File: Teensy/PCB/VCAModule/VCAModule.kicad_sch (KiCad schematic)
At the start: 11 parts, among them J1 Power_Connector_2x3, U1 Teensy4.0

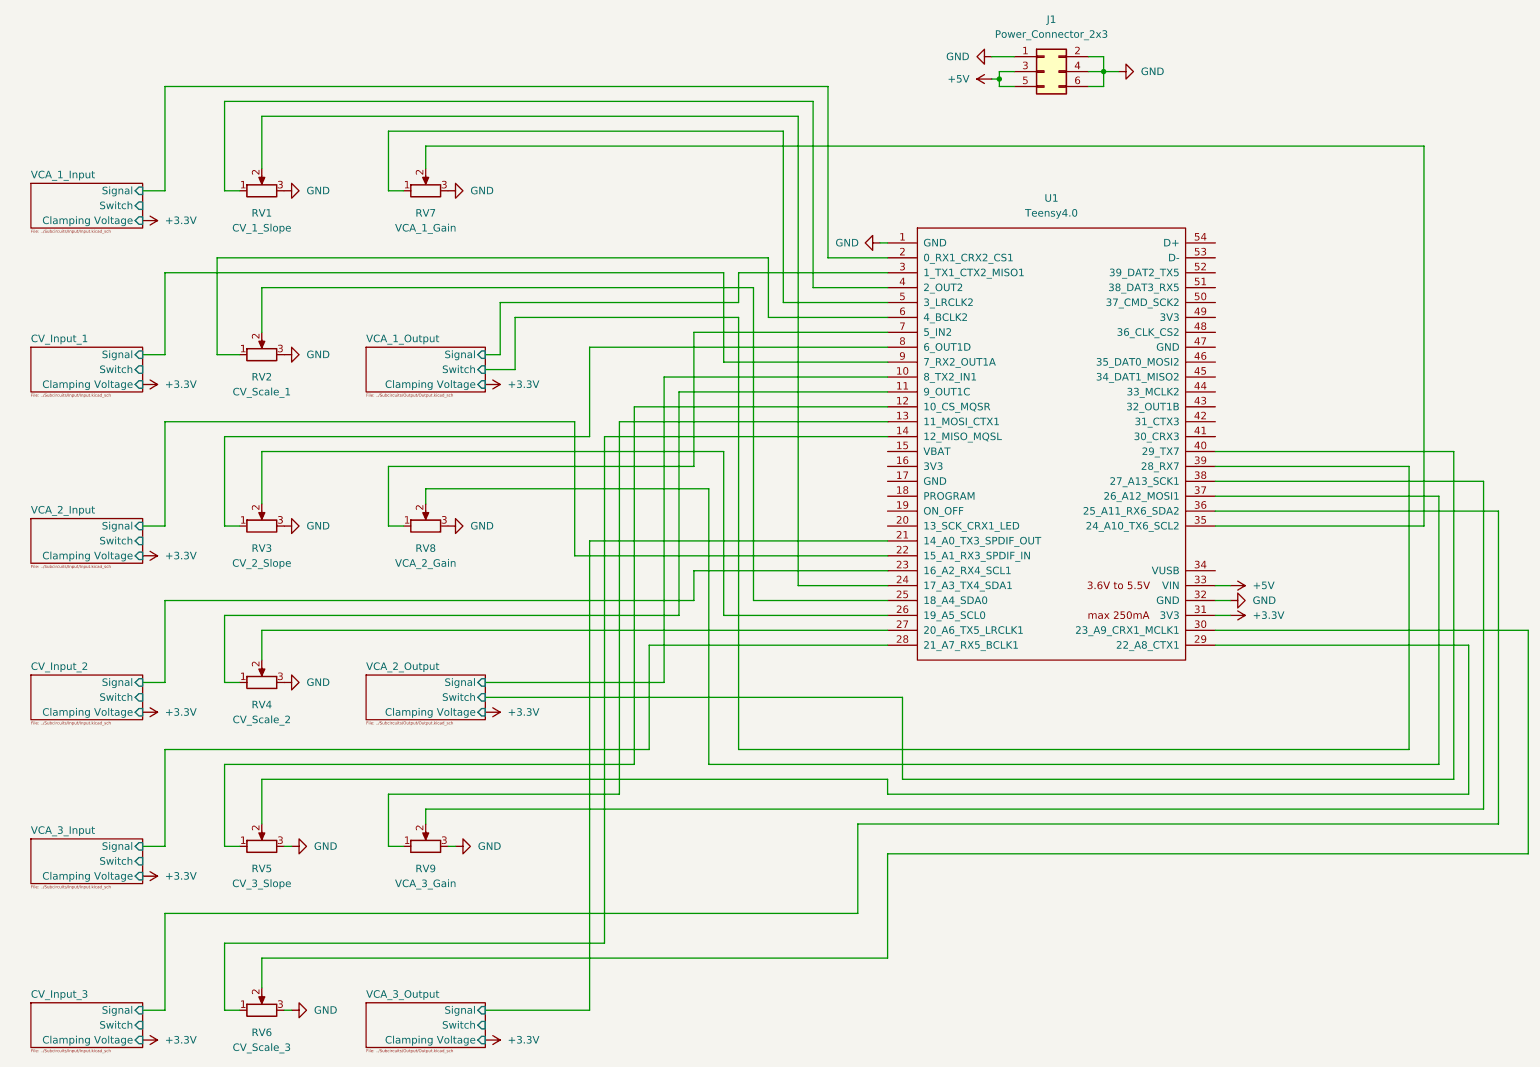
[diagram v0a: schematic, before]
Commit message: Replaced Schematic Lines with references
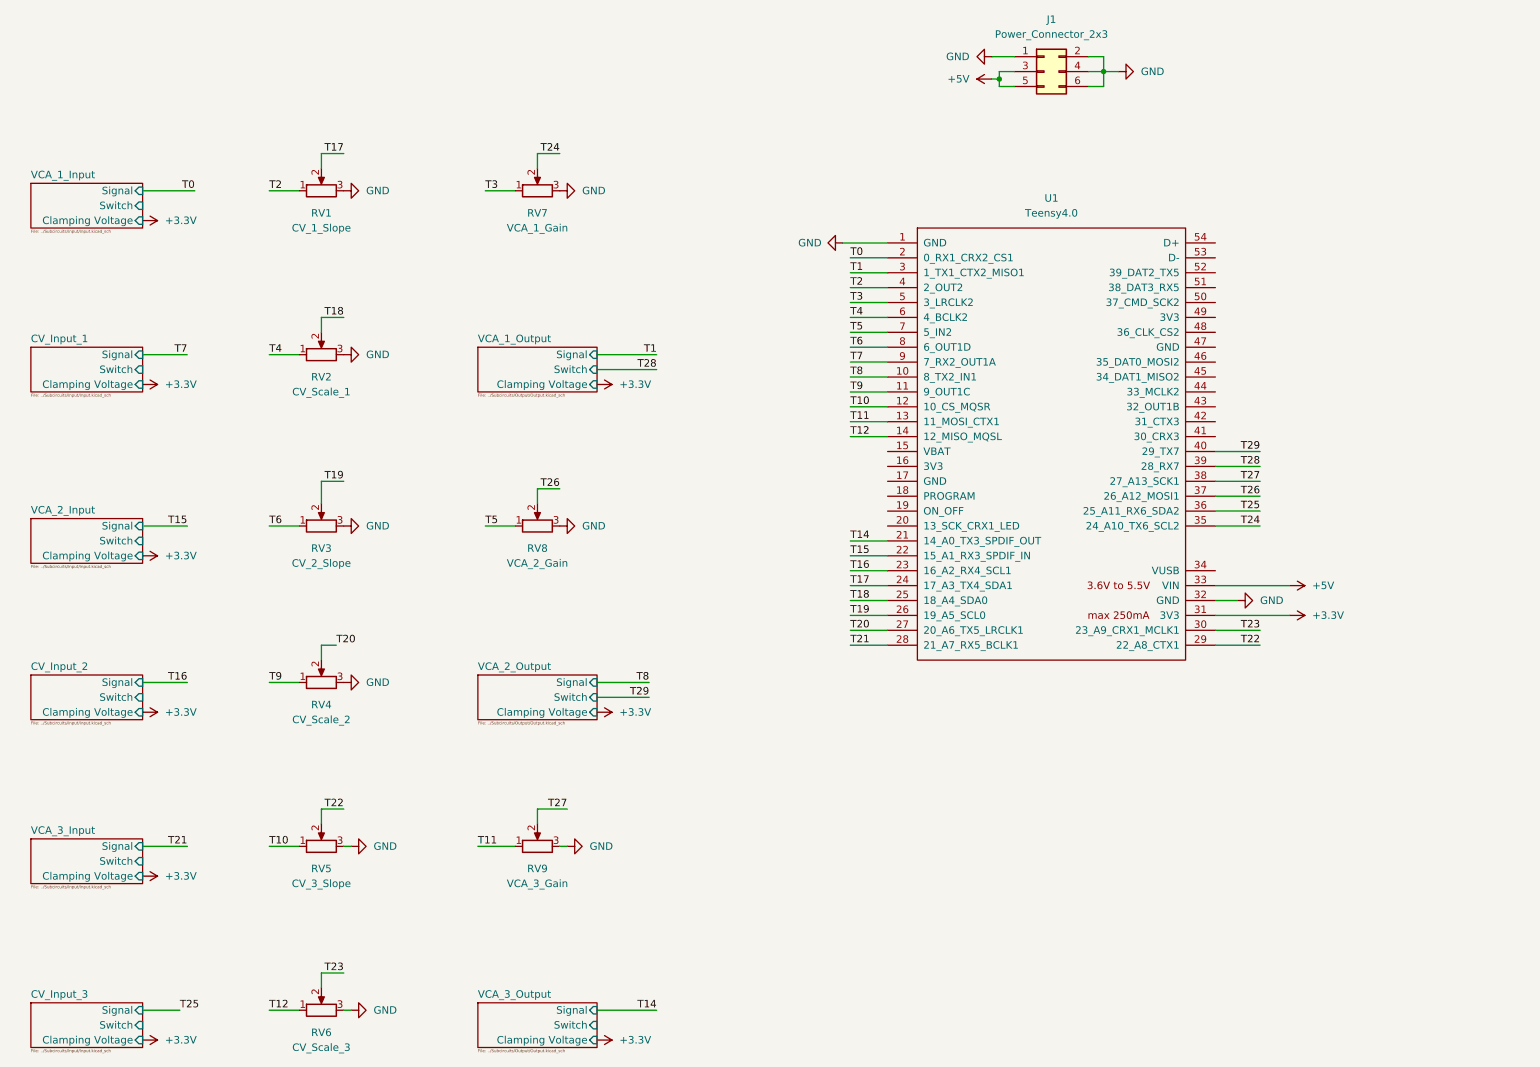
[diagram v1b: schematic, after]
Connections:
- net T3: now reaches RV7.1, U1.5 (3_LRCLK2)
- net T24: now reaches RV7.2, U1.35 (24_A10_TX6_SCL2)
- net T9: now reaches RV4.1, U1.11 (9_OUT1C)
- net T20: now reaches RV4.2, U1.27 (20_A6_TX5_LRCLK1)
- net T4: now reaches RV2.1, U1.6 (4_BCLK2)
- net T18: now reaches RV2.2, U1.25 (18_A4_SDA0)
- net T5: now reaches RV8.1, U1.7 (5_IN2)
- net T26: now reaches RV8.2, U1.37 (26_A12_MOSI1)
- net T10: now reaches RV5.1, U1.12 (10_CS_MQSR)
- net T11: now reaches RV9.1, U1.13 (11_MOSI_CTX1)
- net T12: now reaches RV6.1, U1.14 (12_MISO_MQSL)
- net T17: now reaches RV1.2, U1.24 (17_A3_TX4_SDA1)
- net T19: now reaches RV3.2, U1.26 (19_A5_SCL0)
- net T22: now reaches RV5.2, U1.29 (22_A8_CTX1)
- net T23: now reaches RV6.2, U1.30 (23_A9_CRX1_MCLK1)
- net T27: now reaches RV9.2, U1.38 (27_A13_SCK1)
- net T2: now reaches RV1.1, U1.4 (2_OUT2)
- net T6: now reaches RV3.1, U1.8 (6_OUT1D)
- net CV_Input_1/Signal renamed T7
- net CV_Input_2/Signal renamed T16
- net CV_Input_3/Signal renamed T25
- net VCA_1_Input/Signal renamed T0
- net VCA_1_Output/Signal renamed T1
- net VCA_1_Output/Switch renamed T28
- net VCA_2_Input/Signal renamed T15
- net VCA_2_Output/Signal renamed T8
- net VCA_2_Output/Switch renamed T29
- net VCA_3_Input/Signal renamed T21
- net VCA_3_Output/Signal renamed T14
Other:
- moved on the sheet: RV1, RV2, RV3, RV4, RV5, RV6, RV7, RV8, RV9
